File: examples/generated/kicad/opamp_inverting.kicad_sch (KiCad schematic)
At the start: 6 parts

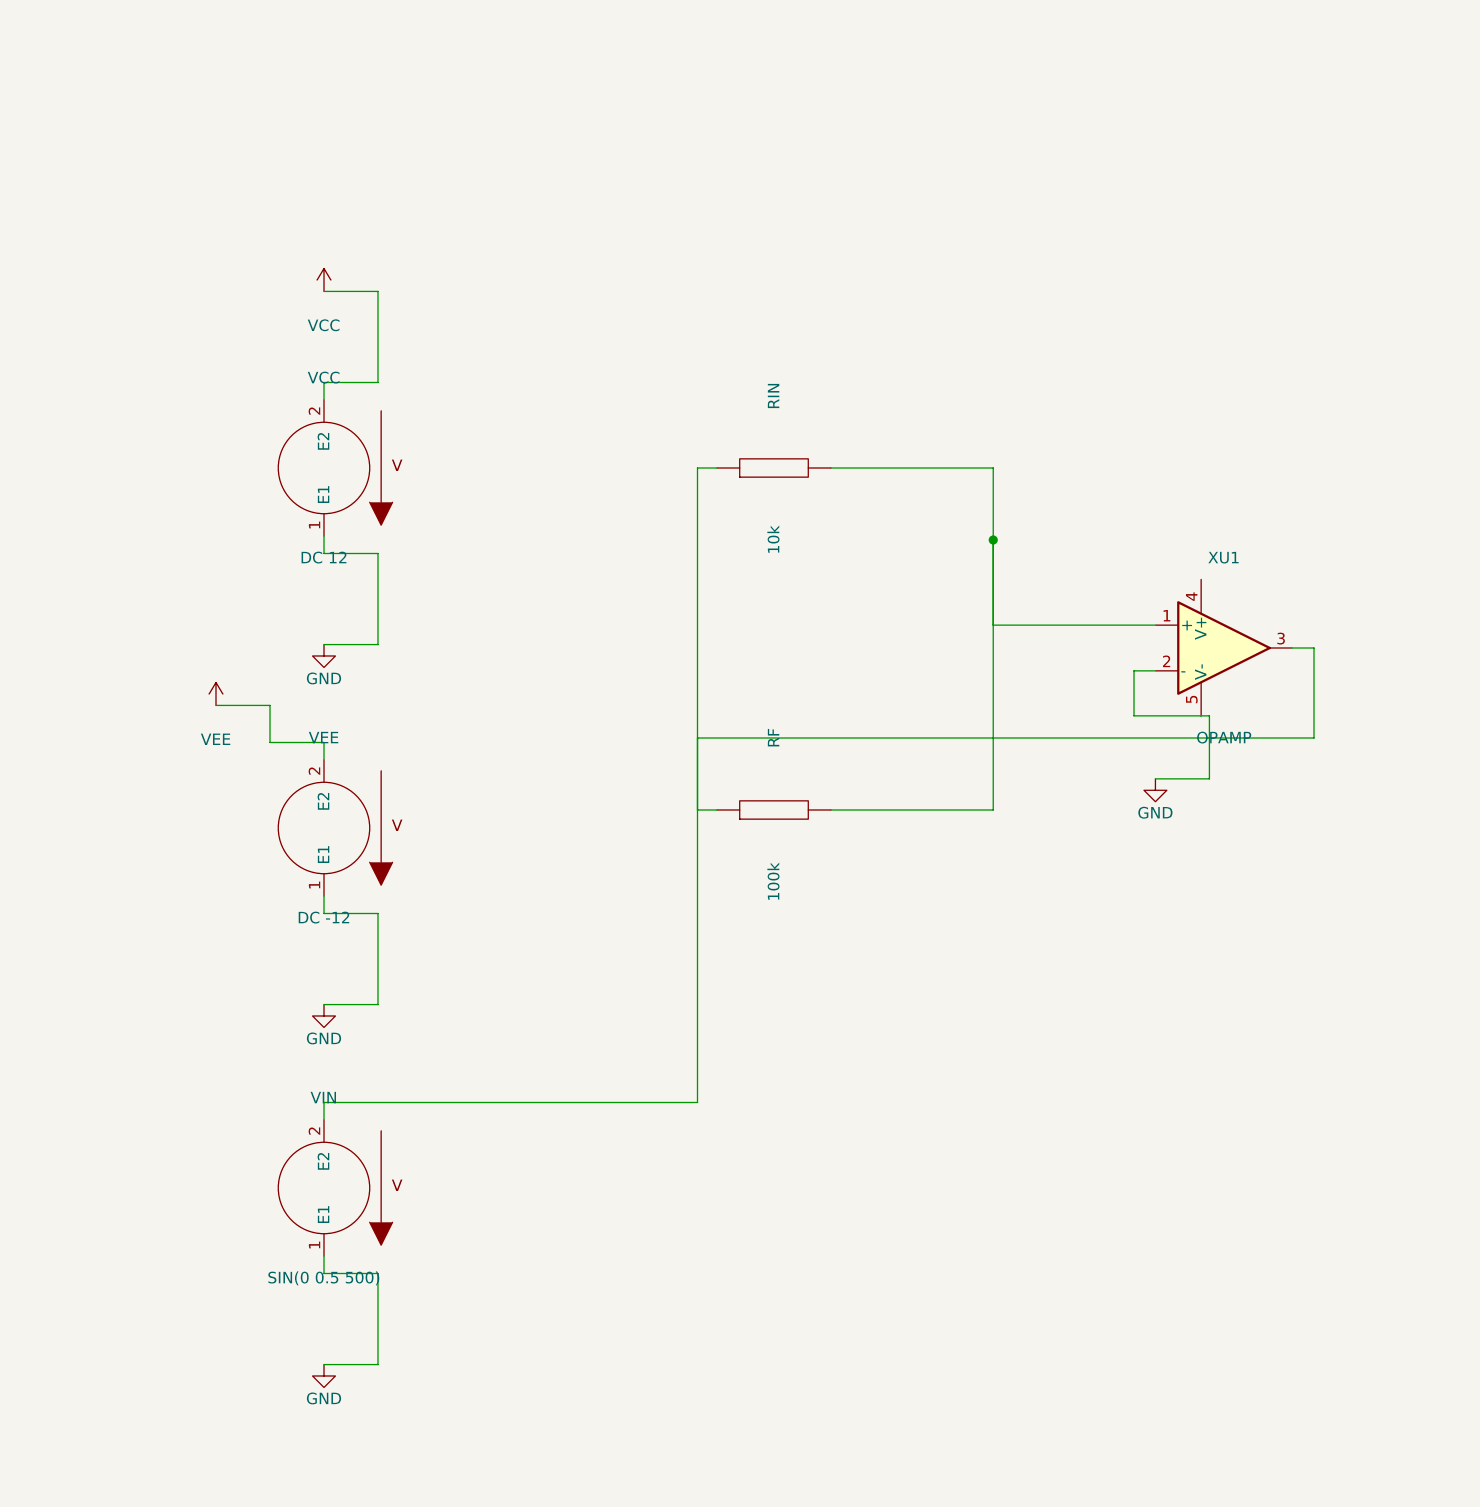
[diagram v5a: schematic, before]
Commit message: Attempt to fix kinking and terminal direction issuses.
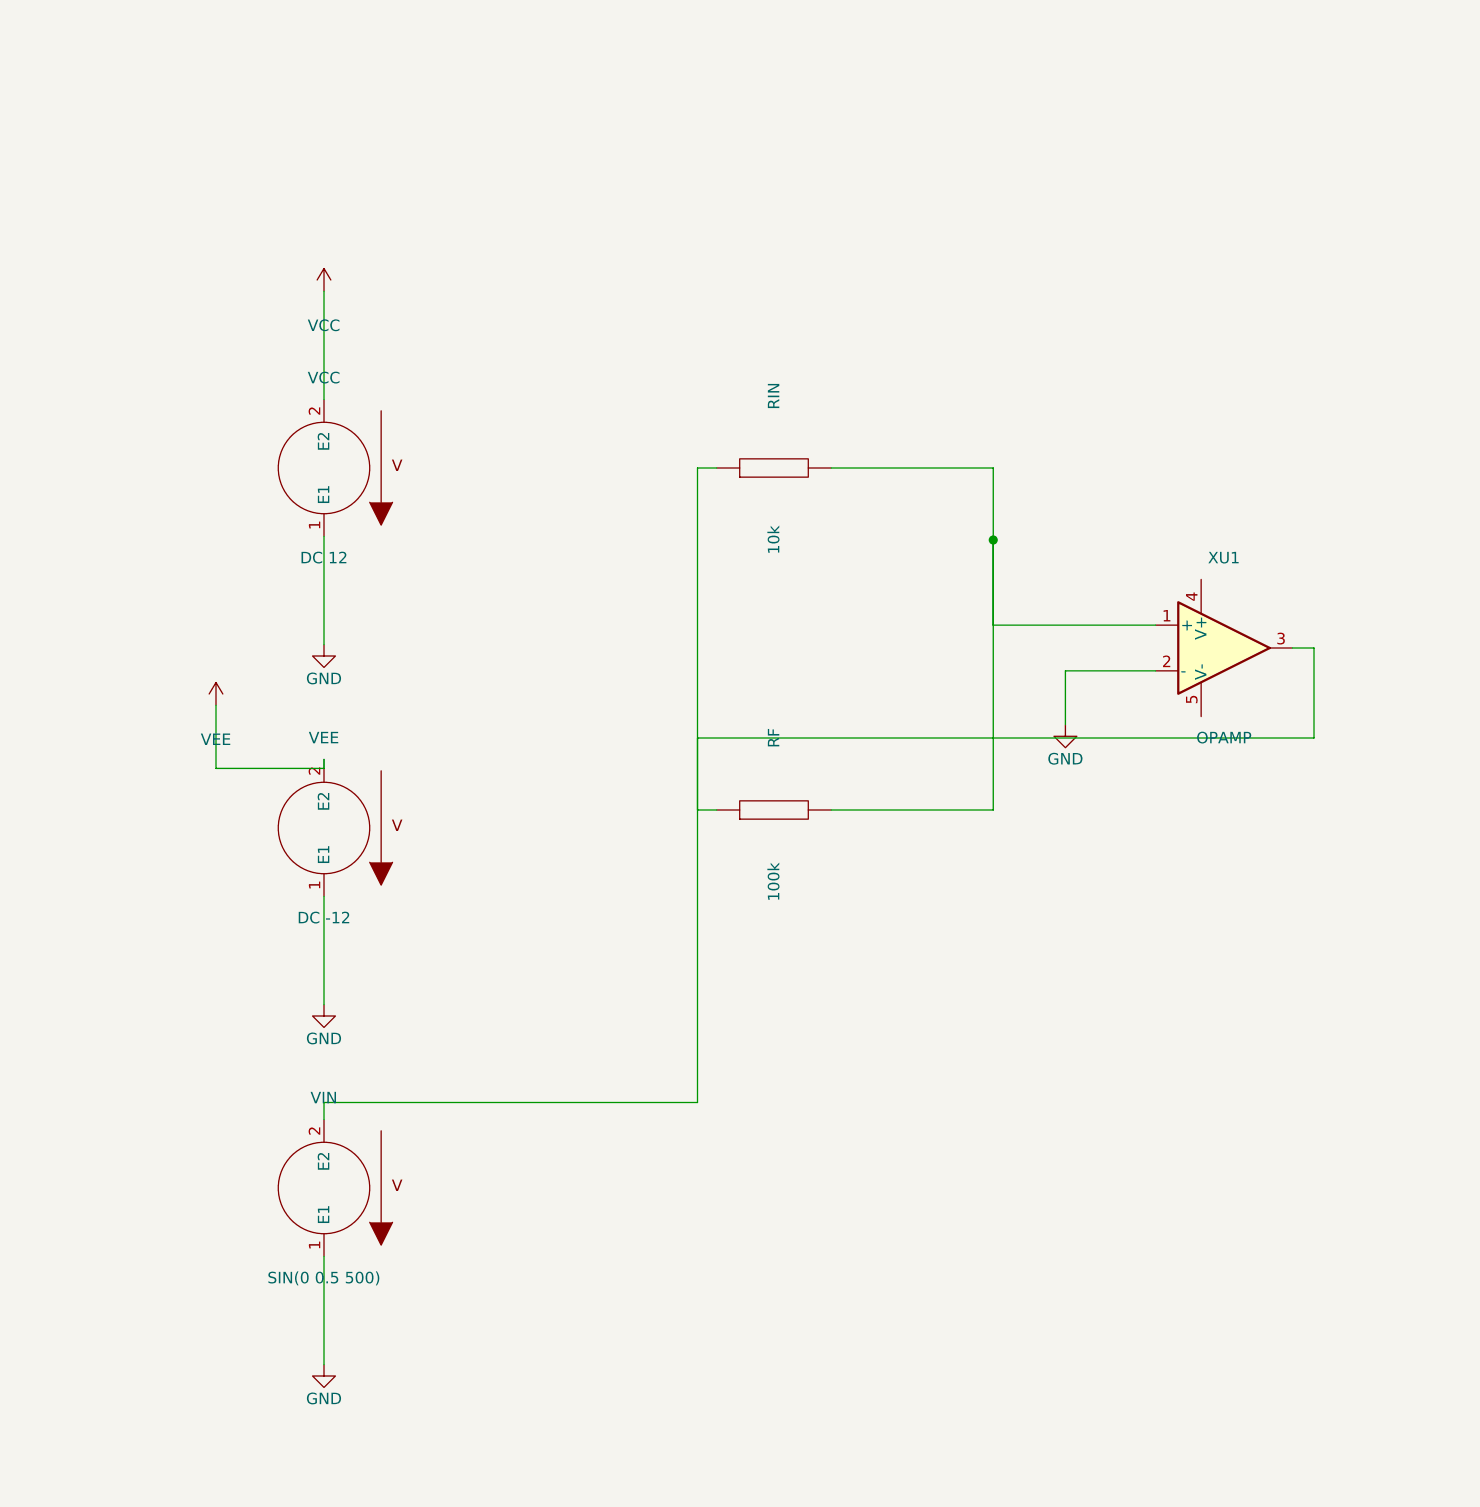
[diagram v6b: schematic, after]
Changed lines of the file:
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@@
     )
   )
-  (symbol (lib_id "GND") (at 144.38 95.92 0) (unit 1)
+  (symbol (lib_id "GND") (at 134.38 89.92 0) (unit 1)
     (in_bom yes) (on_board yes)
-    (property "Reference" "#PWR0006" (at 144.38 92.11 0)
+    (property "Reference" "#PWR0006" (at 134.38 86.11 0)
       (effects (font (size 1.27 1.27)) hide)
     )
-    (property "Value" "GND" (at 144.38 99.73 0)
+    (property "Value" "GND" (at 134.38 93.73 0)
       (effects (font (size 1.27 1.27)))
     )
@@
     )
   )
-  (wire (pts (xy 52.00 53.76) (xy 52.00 51.88))
+  (wire (pts (xy 52.00 53.76) (xy 52.00 41.76))
     (stroke (width 0) (type solid) (color 0 0 0 0))
   )
-  (wire (pts (xy 52.00 51.88) (xy 58.00 51.88))
+  (wire (pts (xy 52.00 69.00) (xy 52.00 81.00))
     (stroke (width 0) (type solid) (color 0 0 0 0))
   )
-  (wire (pts (xy 58.00 51.88) (xy 58.00 41.76))
+  (wire (pts (xy 52.00 93.76) (xy 52.00 94.76))
     (stroke (width 0) (type solid) (color 0 0 0 0))
   )
-  (wire (pts (xy 58.00 41.76) (xy 52.00 41.76))
+  (wire (pts (xy 52.00 94.76) (xy 40.00 94.76))
     (stroke (width 0) (type solid) (color 0 0 0 0))
   )
-  (wire (pts (xy 52.00 69.00) (xy 52.00 70.88))
+  (wire (pts (xy 40.00 94.76) (xy 40.00 87.76))
     (stroke (width 0) (type solid) (color 0 0 0 0))
   )
-  (wire (pts (xy 52.00 70.88) (xy 58.00 70.88))
+  (wire (pts (xy 52.00 109.00) (xy 52.00 121.00))
     (stroke (width 0) (type solid) (color 0 0 0 0))
   )
-  (wire (pts (xy 58.00 70.88) (xy 58.00 81.00))
+  (wire (pts (xy 52.00 149.00) (xy 52.00 161.00))
     (stroke (width 0) (type solid) (color 0 0 0 0))
   )
-  (wire (pts (xy 58.00 81.00) (xy 52.00 81.00))
+  (wire (pts (xy 144.38 83.92) (xy 134.38 83.92))
     (stroke (width 0) (type solid) (color 0 0 0 0))
   )
-  (wire (pts (xy 52.00 93.76) (xy 52.00 91.88))
+  (wire (pts (xy 134.38 83.92) (xy 134.38 89.92))
     (stroke (width 0) (type solid) (color 0 0 0 0))
   )
-  (wire (pts (xy 52.00 91.88) (xy 46.00 91.88))
-    (stroke (width 0) (type solid) (color 0 0 0 0))
-  )
-  (wire (pts (xy 46.00 91.88) (xy 46.00 87.76))
-    (stroke (width 0) (type solid) (color 0 0 0 0))
-  )
-  (wire (pts (xy 46.00 87.76) (xy 40.00 87.76))
-    (stroke (width 0) (type solid) (color 0 0 0 0))
-  )
-  (wire (pts (xy 52.00 109.00) (xy 52.00 110.88))
-    (stroke (width 0) (type solid) (color 0 0 0 0))
-  )
-  (wire (pts (xy 52.00 110.88) (xy 58.00 110.88))
-    (stroke (width 0) (type solid) (color 0 0 0 0))
-  )
-  (wire (pts (xy 58.00 110.88) (xy 58.00 121.00))
-    (stroke (width 0) (type solid) (color 0 0 0 0))
-  )
-  (wire (pts (xy 58.00 121.00) (xy 52.00 121.00))
-    (stroke (width 0) (type solid) (color 0 0 0 0))
-  )
-  (wire (pts (xy 52.00 149.00) (xy 52.00 150.88))
-    (stroke (width 0) (type solid) (color 0 0 0 0))
-  )
-  (wire (pts (xy 52.00 150.88) (xy 58.00 150.88))
-    (stroke (width 0) (type solid) (color 0 0 0 0))
-  )
-  (wire (pts (xy 58.00 150.88) (xy 58.00 161.00))
-    (stroke (width 0) (type solid) (color 0 0 0 0))
-  )
-  (wire (pts (xy 58.00 161.00) (xy 52.00 161.00))
-    (stroke (width 0) (type solid) (color 0 0 0 0))
-  )
-  (wire (pts (xy 144.38 83.92) (xy 142.00 83.92))
-    (stroke (width 0) (type solid) (color 0 0 0 0))
-  )
-  (wire (pts (xy 142.00 83.92) (xy 142.00 88.92))
-    (stroke (width 0) (type solid) (color 0 0 0 0))
-  )
-  (wire (pts (xy 142.00 88.92) (xy 150.38 88.92))
-    (stroke (width 0) (type solid) (color 0 0 0 0))
-  )
-  (wire (pts (xy 150.38 88.92) (xy 150.38 95.92))
-    (stroke (width 0) (type solid) (color 0 0 0 0))
-  )
-  (wire (pts (xy 150.38 95.92) (xy 144.38 95.92))
-    (stroke (width 0) (type solid) (color 0 0 0 0))
-  )

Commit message: Attempt to fix more terminal issues.
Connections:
- net at RIN.2, XU1.1 (+): now also RF.1; no longer RF.2
- net at RIN.1, VIN.2 (E2): no longer RF.1, XU1.3
- net VCC: no longer names the net of VCC.2 (E2)
- net VEE: no longer names the net of VEE.2 (E2)
- new net: RF.2, XU1.3
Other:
- moved on the sheet: RF, RIN, VCC, VEE, VIN, XU1
